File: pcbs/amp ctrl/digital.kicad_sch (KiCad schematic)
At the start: 95 parts, among them J14 RF_Shield_Two_Pieces, U11 LT1880, U6 LTC6220/LT6202, U8 AD5676, U90 ADS8168/ADS8167

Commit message: Amp ctrl: lengthened ADC & DAC reset delay to ~50 ms (#14) Backplane: added clock multiplier for 10 Mhz scanner clock (fixes #21) Backplane: reduced R5 from 10 to 1 ohm, to avoid excessive voltage drop (#20) Backplane: replaced 15V regulator with efficient voltage limiter (#20) Backplane: changed all mounting holes to signal ground Backplane: replaced +2.5V regulator with a higher-current model to support FPGA I/O bank current draw Updated to KiCAD 8
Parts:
- R24, R46, R47, R48, R49, R50, R51, R52: now not fitted

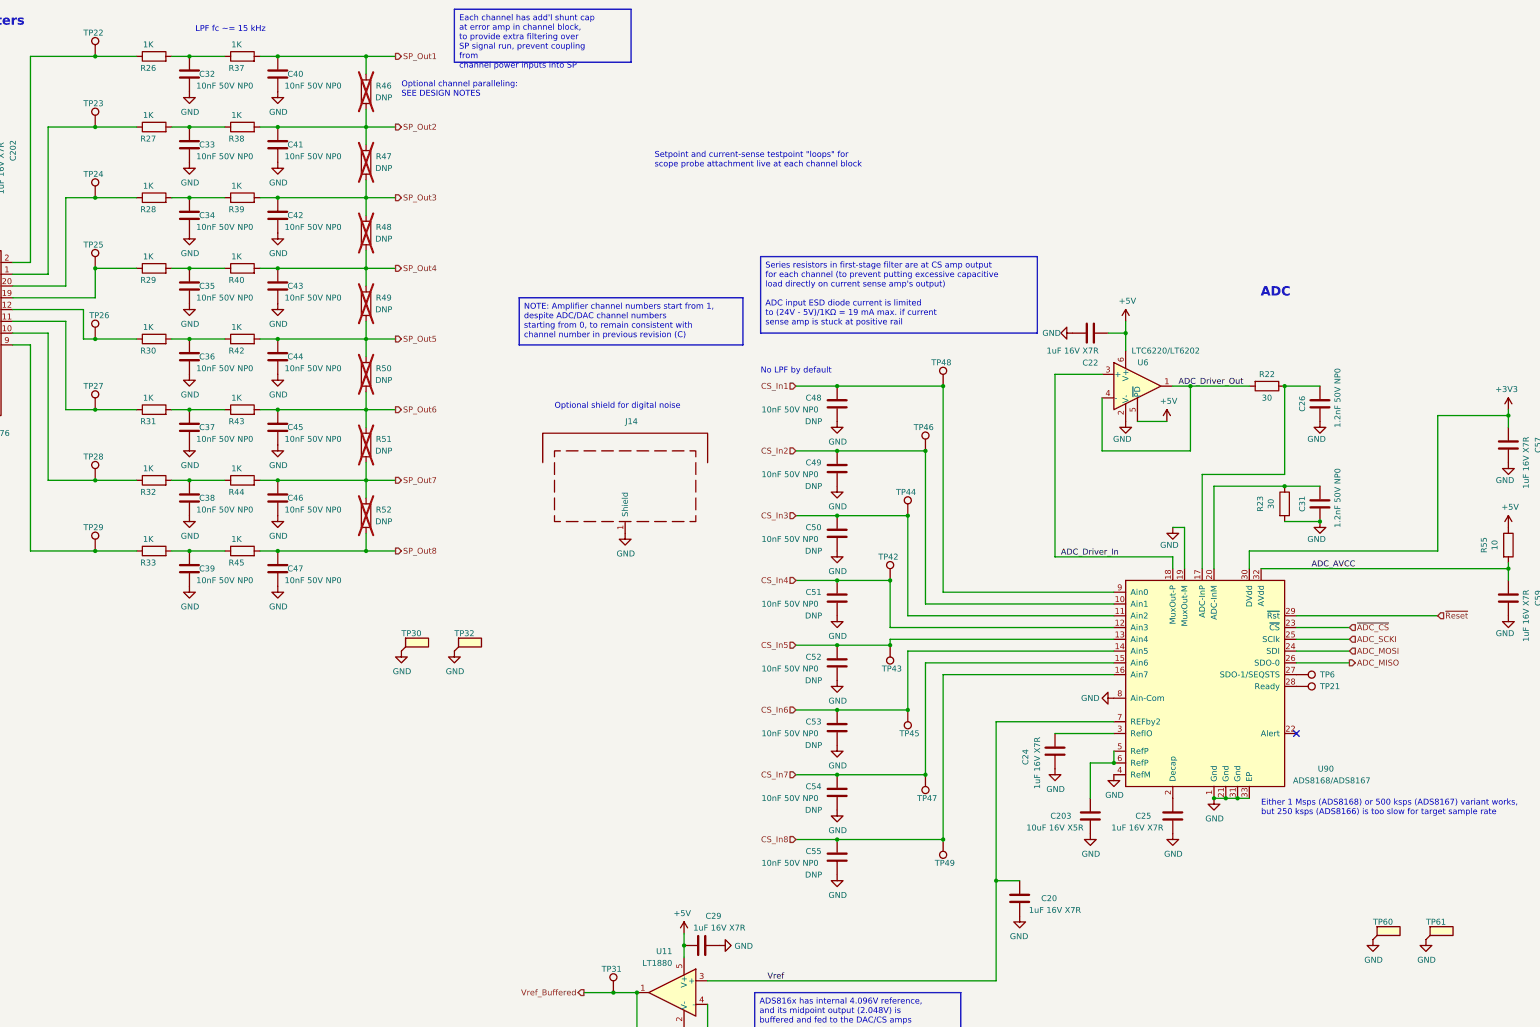
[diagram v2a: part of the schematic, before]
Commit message: Misc. cleanup for mfg & improvements
Minor backplane pinout doc corrections (SCKO5 polarity, clarified some descriptions)
Backplane: Added differential- and common-mode (to standoffs) power filtering, for EMI escaping over power wiring
Amp ctrl: Changed DAC testpoints from individual pads to Keystone 5019 for easier probing
Corrected part numbers, DNP vs. non-BOM-item indications, other misc. BOM issues
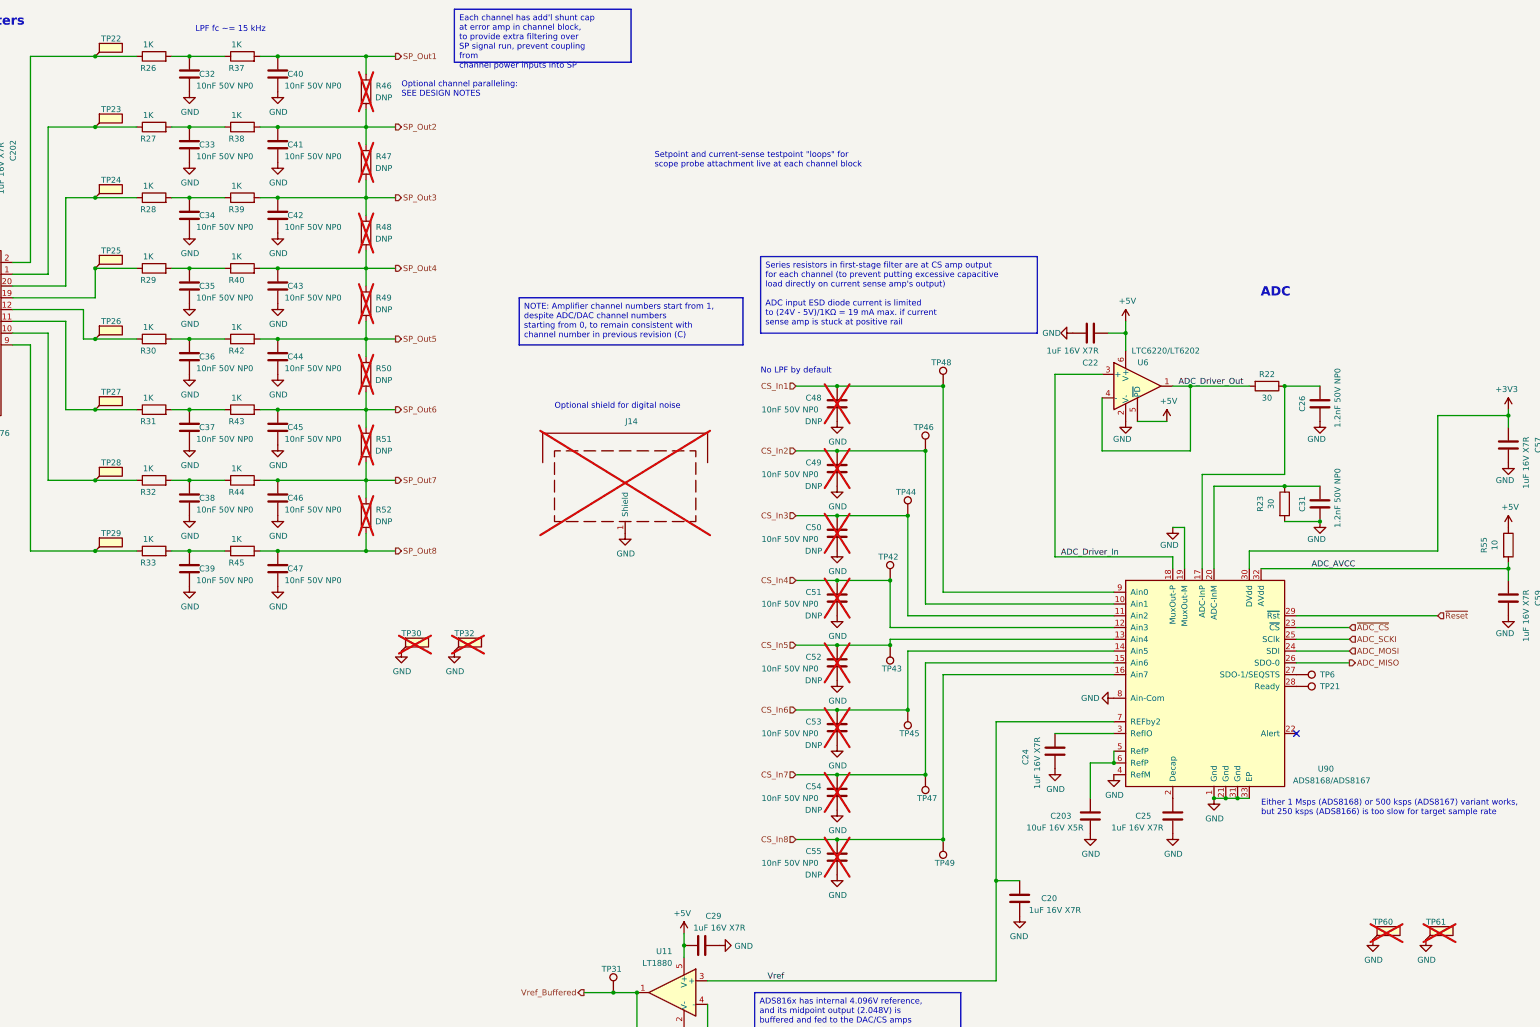
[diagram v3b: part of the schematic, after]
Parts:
- C48, C49, C50, C51, C52, C53, C54, C55, J14: now not fitted
- TP21, TP6: now left out of the parts list
- TP22, TP23, TP24, TP25, TP26, TP27, TP28, TP29: footprint TestPoint:TestPoint_Pad_1.0x1.0mm -> Don_std:TestPoint_Keystone_5019_Minature; symbol Connector:TestPoint -> Connector:TestPoint_Flag; Manufacturer (none) -> Keystone; Part Number (none) -> 5019; now in the parts list
- TP30, TP32, TP60, TP61: footprint TestPoint:TestPoint_Keystone_5019_Minature -> Don_std:TestPoint_Keystone_5019_Minature; now not fitted

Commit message: Moved all project-specific symbols & footprints into new "shim" libraries Updated projects to reference the new "shim" library
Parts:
- J14: footprint Don:Shield_Wurth_36107406S_Minimal-inside -> shim:Shield_Wurth_36107406S_Minimal-inside
- TP22, TP23, TP24, TP25, TP26, TP27, TP28, TP29, TP30, TP32, TP60, TP61: footprint Don_std:TestPoint_Keystone_5019_Minature -> TestPoint:TestPoint_Keystone_5019_Minature
- U11: footprint Martinos_std:SOT-23-5 -> Package_TO_SOT_SMD:SOT-23-5
- U6: footprint Martinos_std:SOT-23-6 -> Package_TO_SOT_SMD:SOT-23-6
- U8: footprint Don_std:TSSOP-20_4.4x6.5mm_P0.65mm -> Package_SO:TSSOP-20_4.4x6.5mm_P0.65mm; symbol Don:AD567x -> shim:AD567x
- U90: footprint Martinos_std:VQFN-32-1EP_5x5mm_P0.5mm_EP3.45x3.45mm -> shim:VQFN-32-1EP_5x5mm_P0.5mm_EP3.45x3.45mm
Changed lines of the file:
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@@
 			)
 		)
-		(property "Footprint" "Martinos_std:SOT-23-5"
+		(property "Footprint" "Package_TO_SOT_SMD:SOT-23-5"
 			(at 212.09 227.33 0)
 			(effects
@@
 			)
 		)
-		(property "Footprint" "Don_std:TestPoint_Keystone_5019_Minature"
+		(property "Footprint" "TestPoint:TestPoint_Keystone_5019_Minature"
 			(at 368.3 215.9 0)
 			(effects
@@
 			)
 		)
-		(property "Footprint" "Don_std:TestPoint_Keystone_5019_Minature"
+		(property "Footprint" "TestPoint:TestPoint_Keystone_5019_Minature"
 			(at 379.73 215.9 0)
 			(effects
@@
 			)
 		)
-		(property "Footprint" "Don_std:TestPoint_Keystone_5019_Minature"
+		(property "Footprint" "TestPoint:TestPoint_Keystone_5019_Minature"
 			(at 92.71 25.4 0)
 			(effects
@@
 			)
 		)
-		(property "Footprint" "Don_std:TestPoint_Keystone_5019_Minature"
+		(property "Footprint" "TestPoint:TestPoint_Keystone_5019_Minature"
 			(at 92.71 40.64 0)
 			(effects
@@
 			)
 		)
-		(property "Footprint" "Don_std:TestPoint_Keystone_5019_Minature"
+		(property "Footprint" "TestPoint:TestPoint_Keystone_5019_Minature"
 			(at 92.71 55.88 0)
 			(effects
@@
 			)
 		)
-		(property "Footprint" "Don_std:TestPoint_Keystone_5019_Minature"
+		(property "Footprint" "TestPoint:TestPoint_Keystone_5019_Minature"
 			(at 92.71 71.12 0)
 			(effects
@@
 			)
 		)
-		(property "Footprint" "Don_std:TestPoint_Keystone_5019_Minature"
+		(property "Footprint" "TestPoint:TestPoint_Keystone_5019_Minature"
 			(at 92.71 86.36 0)
 			(effects
@@
 			)
 		)
-		(property "Footprint" "Don_std:TestPoint_Keystone_5019_Minature"
+		(property "Footprint" "TestPoint:TestPoint_Keystone_5019_Minature"
 			(at 92.71 101.6 0)
 			(effects
@@
 			)
 		)
-		(property "Footprint" "Don_std:TestPoint_Keystone_5019_Minature"
+		(property "Footprint" "TestPoint:TestPoint_Keystone_5019_Minature"
 			(at 92.71 116.84 0)
 			(effects
@@
 			)
 		)
-		(property "Footprint" "Don_std:TestPoint_Keystone_5019_Minature"
+		(property "Footprint" "TestPoint:TestPoint_Keystone_5019_Minature"
 			(at 92.71 132.08 0)
 			(effects
@@
 			)
 		)
-		(property "Footprint" "Don_std:TestPoint_Keystone_5019_Minature"
+		(property "Footprint" "TestPoint:TestPoint_Keystone_5019_Minature"
 			(at 158.75 153.67 0)
 			(effects
@@
 			)
 		)
-		(property "Footprint" "Don_std:TestPoint_Keystone_5019_Minature"
+		(property "Footprint" "TestPoint:TestPoint_Keystone_5019_Minature"
 			(at 170.18 153.67 0)
 			(effects
@@
 			)
 		)
-		(property "Footprint" "Don:Shield_Wurth_36107406S_Minimal-inside"
+		(property "Footprint" "shim:Shield_Wurth_36107406S_Minimal-inside"
 			(at 201.93 120.65 0)
 			(effects
@@
 			)
 		)
-		(property "Footprint" "Martinos_std:VQFN-32-1EP_5x5mm_P0.5mm_EP3.45x3.45mm"
+		(property "Footprint" "shim:VQFN-32-1EP_5x5mm_P0.5mm_EP3.45x3.45mm"
 			(at 323.85 135.89 0)
 			(effects
@@
 			)
 		)
-		(property "Footprint" "Martinos_std:SOT-23-6"
+		(property "Footprint" "Package_TO_SOT_SMD:SOT-23-6"
 			(at 312.42 111.76 0)
 			(effects
@@
 	)
 	(symbol
-		(lib_id "Don:AD567x")
+		(lib_id "shim:AD567x")
 		(at 54.61 83.82 0)
 		(unit 1)
@@
 			)
 		)
-		(property "Footprint" "Don_std:TSSOP-20_4.4x6.5mm_P0.65mm"
+		(property "Footprint" "Package_SO:TSSOP-20_4.4x6.5mm_P0.65mm"
 			(at 59.69 62.23 0)
 			(effects

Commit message: Finished migrating footprint names
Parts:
- TP22, TP23, TP24, TP25, TP26, TP27, TP28, TP29, TP30, TP32, TP60, TP61: footprint TestPoint:TestPoint_Keystone_5019_Minature -> TestPoint:TestPoint_Keystone_5019_Miniature
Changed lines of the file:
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@@
 			)
 		)
-		(property "Footprint" "TestPoint:TestPoint_Keystone_5019_Minature"
+		(property "Footprint" "TestPoint:TestPoint_Keystone_5019_Miniature"
 			(at 368.3 215.9 0)
 			(effects
@@
 			)
 		)
-		(property "Footprint" "TestPoint:TestPoint_Keystone_5019_Minature"
+		(property "Footprint" "TestPoint:TestPoint_Keystone_5019_Miniature"
 			(at 379.73 215.9 0)
 			(effects
@@
 			)
 		)
-		(property "Footprint" "TestPoint:TestPoint_Keystone_5019_Minature"
+		(property "Footprint" "TestPoint:TestPoint_Keystone_5019_Miniature"
 			(at 92.71 25.4 0)
 			(effects
@@
 			)
 		)
-		(property "Footprint" "TestPoint:TestPoint_Keystone_5019_Minature"
+		(property "Footprint" "TestPoint:TestPoint_Keystone_5019_Miniature"
 			(at 92.71 40.64 0)
 			(effects
@@
 			)
 		)
-		(property "Footprint" "TestPoint:TestPoint_Keystone_5019_Minature"
+		(property "Footprint" "TestPoint:TestPoint_Keystone_5019_Miniature"
 			(at 92.71 55.88 0)
 			(effects
@@
 			)
 		)
-		(property "Footprint" "TestPoint:TestPoint_Keystone_5019_Minature"
+		(property "Footprint" "TestPoint:TestPoint_Keystone_5019_Miniature"
 			(at 92.71 71.12 0)
 			(effects
@@
 			)
 		)
-		(property "Footprint" "TestPoint:TestPoint_Keystone_5019_Minature"
+		(property "Footprint" "TestPoint:TestPoint_Keystone_5019_Miniature"
 			(at 92.71 86.36 0)
 			(effects
@@
 			)
 		)
-		(property "Footprint" "TestPoint:TestPoint_Keystone_5019_Minature"
+		(property "Footprint" "TestPoint:TestPoint_Keystone_5019_Miniature"
 			(at 92.71 101.6 0)
 			(effects
@@
 			)
 		)
-		(property "Footprint" "TestPoint:TestPoint_Keystone_5019_Minature"
+		(property "Footprint" "TestPoint:TestPoint_Keystone_5019_Miniature"
 			(at 92.71 116.84 0)
 			(effects
@@
 			)
 		)
-		(property "Footprint" "TestPoint:TestPoint_Keystone_5019_Minature"
+		(property "Footprint" "TestPoint:TestPoint_Keystone_5019_Miniature"
 			(at 92.71 132.08 0)
 			(effects
@@
 			)
 		)
-		(property "Footprint" "TestPoint:TestPoint_Keystone_5019_Minature"
+		(property "Footprint" "TestPoint:TestPoint_Keystone_5019_Miniature"
 			(at 158.75 153.67 0)
 			(effects
@@
 			)
 		)
-		(property "Footprint" "TestPoint:TestPoint_Keystone_5019_Minature"
+		(property "Footprint" "TestPoint:TestPoint_Keystone_5019_Miniature"
 			(at 170.18 153.67 0)
 			(effects

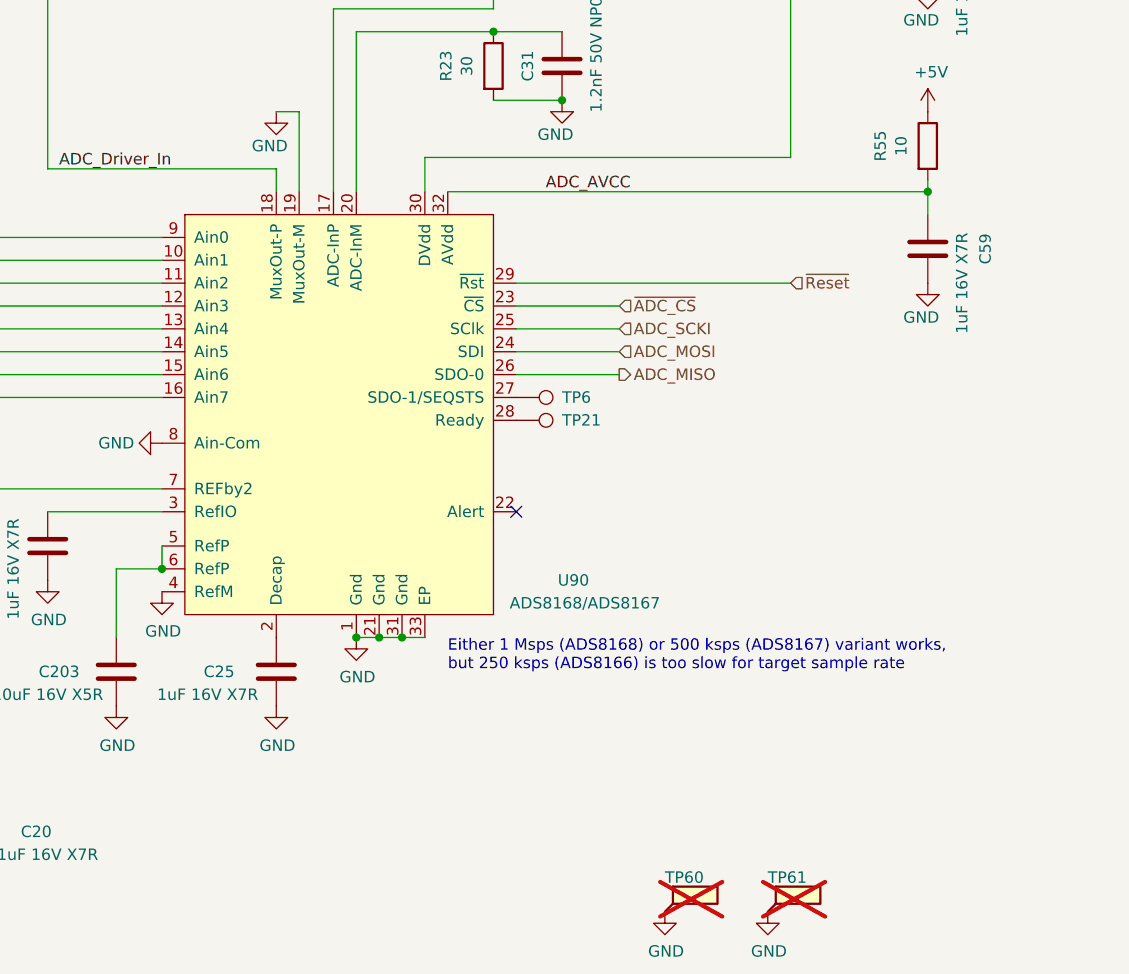
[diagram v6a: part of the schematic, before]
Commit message: Functional fixes for ADC clk, +3.3V sag on backplane
Amp ctrl: Added ADC clock inversion (fixes #34)
Backplane: fixed series-resistor-induced voltage sag (fixes #33)
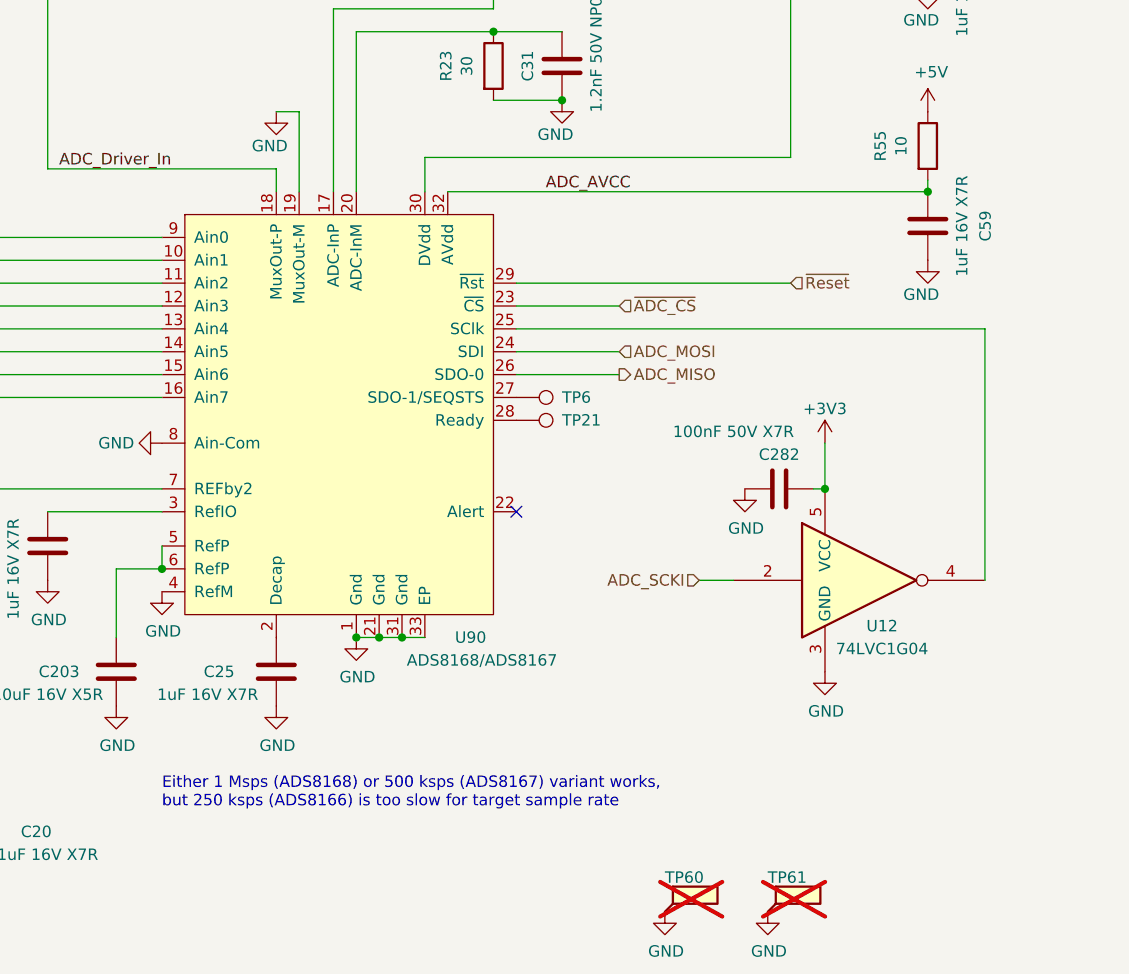
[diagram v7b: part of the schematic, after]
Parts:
- added C282: 100nF 50V X7R, Capacitor_SMD:C_0603_1608Metric, symbol Device:C
- added U12: 74LVC1G04, Package_TO_SOT_SMD:SOT-23-5, symbol 74xGxx:74LVC1G04
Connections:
- net +3V3: now also C282.1, U12.5 (VCC)
- net ADC_SCKI: now also U12.2; no longer U90.25 (SClk)
- net GND: now also C282.2, U12.3 (GND)
- new net: U12.4, U90.25 (SClk)
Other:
- moved on the sheet: C59
